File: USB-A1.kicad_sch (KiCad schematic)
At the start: 26 parts, among them J8 USB3_A, J9 USB3_A, U16 UCS2113-1-V/G4, U17 TPD4E02B04DQA, U18 TPD4E02B04DQA

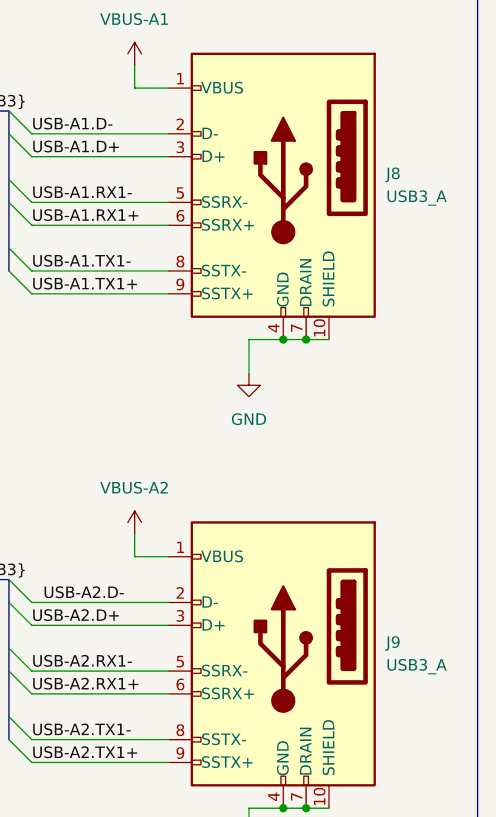
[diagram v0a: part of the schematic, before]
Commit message: TPS25762 EEPROM connector added
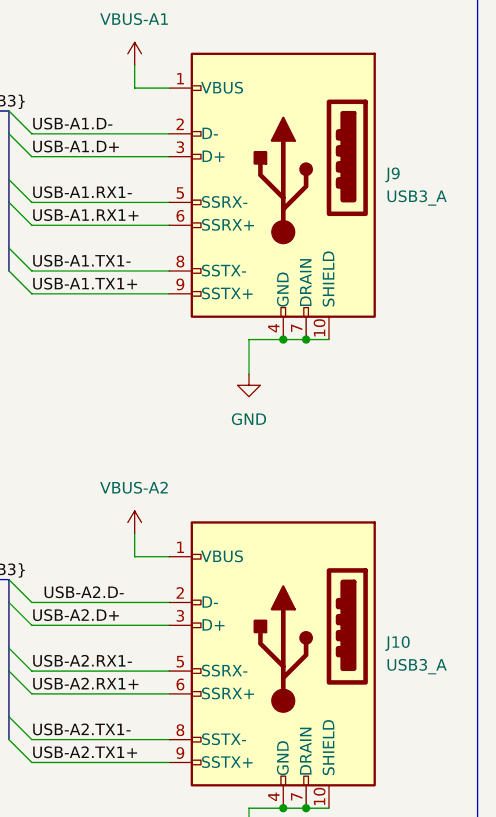
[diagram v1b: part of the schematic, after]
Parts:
- renumbered J9 to J10, J8 to J9
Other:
- title: (none) -> USB Hub
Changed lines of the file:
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@@
 	(generator_version "9.0")
 	(paper "A4")
+	(title_block
+		(title "USB Hub")
+	)
 	(rectangle
 		(start 15.24 71.12)
@@
 		(dnp no)
 		(fields_autoplaced yes)
-		(property "Reference" "J8"
+		(property "Reference" "J9"
 			(at 273.05 40.0049 0)
 			(effects
@@
 			(project ""
 				(path "/a2586c28-95f1-49e6-9254-37d7a8473e53/10c83c9e-05bd-4fa1-b7e1-a721413825c3"
-					(reference "J8")
+					(reference "J9")
 					(unit 1)
 				)
@@
 		(dnp no)
 		(fields_autoplaced yes)
-		(property "Reference" "J9"
+		(property "Reference" "J10"
 			(at 273.05 92.0749 0)
 			(effects
@@
 			(project "USB_hub"
 				(path "/a2586c28-95f1-49e6-9254-37d7a8473e53/10c83c9e-05bd-4fa1-b7e1-a721413825c3"
-					(reference "J9")
+					(reference "J10")
 					(unit 1)
 				)

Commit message: deleted duplicated capacitor
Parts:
- C77, C78, C79, C80: footprint (none) -> Capacitor_THT:C_Radial_D10.0mm_H16.0mm_P5.00mm
- C81: footprint (none) -> Capacitor_SMD:C_0402_1005Metric
- J10, J9: footprint (none) -> Connector_USB:USB3_A_Molex_48393-001
- JP2, JP3: footprint (none) -> Jumper:SolderJumper-2_P1.3mm_Open_Pad1.0x1.5mm
- JP4: footprint (none) -> Jumper:SolderJumper-3_P1.3mm_Open_RoundedPad1.0x1.5mm_NumberLabels
- R45, R46, R47, R48, R49, R50, R51: footprint (none) -> Resistor_SMD:R_0603_1608Metric
- TP5, TP6: footprint (none) -> TestPoint:TestPoint_THTPad_1.5x1.5mm_Drill0.7mm
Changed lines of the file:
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@@
 			)
 		)
-		(property "Footprint" ""
+		(property "Footprint" "Resistor_SMD:R_0603_1608Metric"
 			(at 54.61 92.202 90)
 			(effects
@@
 			)
 		)
-		(property "Footprint" ""
+		(property "Footprint" "Resistor_SMD:R_0603_1608Metric"
 			(at 29.972 35.56 90)
 			(effects
@@
 			)
 		)
-		(property "Footprint" ""
+		(property "Footprint" "Capacitor_THT:C_Radial_D10.0mm_H16.0mm_P5.00mm"
 			(at 108.9152 26.67 0)
 			(effects
@@
 			)
 		)
-		(property "Footprint" ""
+		(property "Footprint" "Connector_USB:USB3_A_Molex_48393-001"
 			(at 257.81 38.1 0)
 			(effects
@@
 			)
 		)
-		(property "Footprint" ""
+		(property "Footprint" "Capacitor_SMD:C_0402_1005Metric"
 			(at 124.1552 26.67 0)
 			(effects
@@
 			)
 		)
-		(property "Footprint" ""
+		(property "Footprint" "Resistor_SMD:R_0603_1608Metric"
 			(at 47.498 24.13 90)
 			(effects
@@
 			)
 		)
-		(property "Footprint" ""
+		(property "Footprint" "TestPoint:TestPoint_THTPad_1.5x1.5mm_Drill0.7mm"
 			(at 101.6 82.55 0)
 			(effects
@@
 			)
 		)
-		(property "Footprint" ""
+		(property "Footprint" "Capacitor_THT:C_Radial_D10.0mm_H16.0mm_P5.00mm"
 			(at 116.5352 26.67 0)
 			(effects
@@
 			)
 		)
-		(property "Footprint" ""
+		(property "Footprint" "Resistor_SMD:R_0603_1608Metric"
 			(at 100.33 46.482 90)
 			(effects
@@
 			)
 		)
-		(property "Footprint" ""
+		(property "Footprint" "TestPoint:TestPoint_THTPad_1.5x1.5mm_Drill0.7mm"
 			(at 80.01 82.55 0)
 			(effects
@@
 			)
 		)
-		(property "Footprint" ""
+		(property "Footprint" "Resistor_SMD:R_0603_1608Metric"
 			(at 88.9 47.498 90)
 			(effects
@@
 			)
 		)
-		(property "Footprint" ""
+		(property "Footprint" "Capacitor_THT:C_Radial_D10.0mm_H16.0mm_P5.00mm"
 			(at 93.6752 26.67 0)
 			(effects
@@
 			)
 		)
-		(property "Footprint" ""
+		(property "Footprint" "Capacitor_THT:C_Radial_D10.0mm_H16.0mm_P5.00mm"
 			(at 101.2952 26.67 0)
 			(effects
@@
 			)
 		)
-		(property "Footprint" ""
+		(property "Footprint" "Connector_USB:USB3_A_Molex_48393-001"
 			(at 257.81 90.17 0)
 			(effects
@@
 			)
 		)
-		(property "Footprint" ""
+		(property "Footprint" "Jumper:SolderJumper-2_P1.3mm_Open_Pad1.0x1.5mm"
 			(at 88.9 40.64 0)
 			(effects
@@
 			)
 		)
-		(property "Footprint" ""
+		(property "Footprint" "Resistor_SMD:R_0603_1608Metric"
 			(at 54.61 76.962 90)
 			(effects
@@
 			)
 		)
-		(property "Footprint" ""
+		(property "Footprint" "Jumper:SolderJumper-2_P1.3mm_Open_Pad1.0x1.5mm"
 			(at 88.9 43.18 0)
 			(effects
@@
 			)
 		)
-		(property "Footprint" ""
+		(property "Footprint" "Jumper:SolderJumper-3_P1.3mm_Open_RoundedPad1.0x1.5mm_NumberLabels"
 			(at 45.72 86.36 0)
 			(effects
@@
 			)
 		)
-		(property "Footprint" ""
+		(property "Footprint" "Resistor_SMD:R_0603_1608Metric"
 			(at 85.598 31.75 90)
 			(effects

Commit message: Minor fixes
Fixed unclear labelling of buses
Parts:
- R45, R46, R47, R48, R49, R50, R51: footprint Resistor_SMD:R_0603_1608Metric -> Resistor_SMD:R_0402_1005Metric
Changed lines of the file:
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@@
 			)
 		)
-		(property "Footprint" "Resistor_SMD:R_0603_1608Metric"
+		(property "Footprint" "Resistor_SMD:R_0402_1005Metric"
 			(at 54.61 92.202 90)
 			(effects
@@
 			)
 		)
-		(property "Footprint" "Resistor_SMD:R_0603_1608Metric"
+		(property "Footprint" "Resistor_SMD:R_0402_1005Metric"
 			(at 29.972 35.56 90)
 			(effects
@@
 			)
 		)
-		(property "Footprint" "Resistor_SMD:R_0603_1608Metric"
+		(property "Footprint" "Resistor_SMD:R_0402_1005Metric"
 			(at 47.498 24.13 90)
 			(effects
@@
 			)
 		)
-		(property "Footprint" "Resistor_SMD:R_0603_1608Metric"
+		(property "Footprint" "Resistor_SMD:R_0402_1005Metric"
 			(at 100.33 46.482 90)
 			(effects
@@
 			)
 		)
-		(property "Footprint" "Resistor_SMD:R_0603_1608Metric"
+		(property "Footprint" "Resistor_SMD:R_0402_1005Metric"
 			(at 88.9 47.498 90)
 			(effects
@@
 			)
 		)
-		(property "Footprint" "Resistor_SMD:R_0603_1608Metric"
+		(property "Footprint" "Resistor_SMD:R_0402_1005Metric"
 			(at 54.61 76.962 90)
 			(effects
@@
 			)
 		)
-		(property "Footprint" "Resistor_SMD:R_0603_1608Metric"
+		(property "Footprint" "Resistor_SMD:R_0402_1005Metric"
 			(at 85.598 31.75 90)
 			(effects

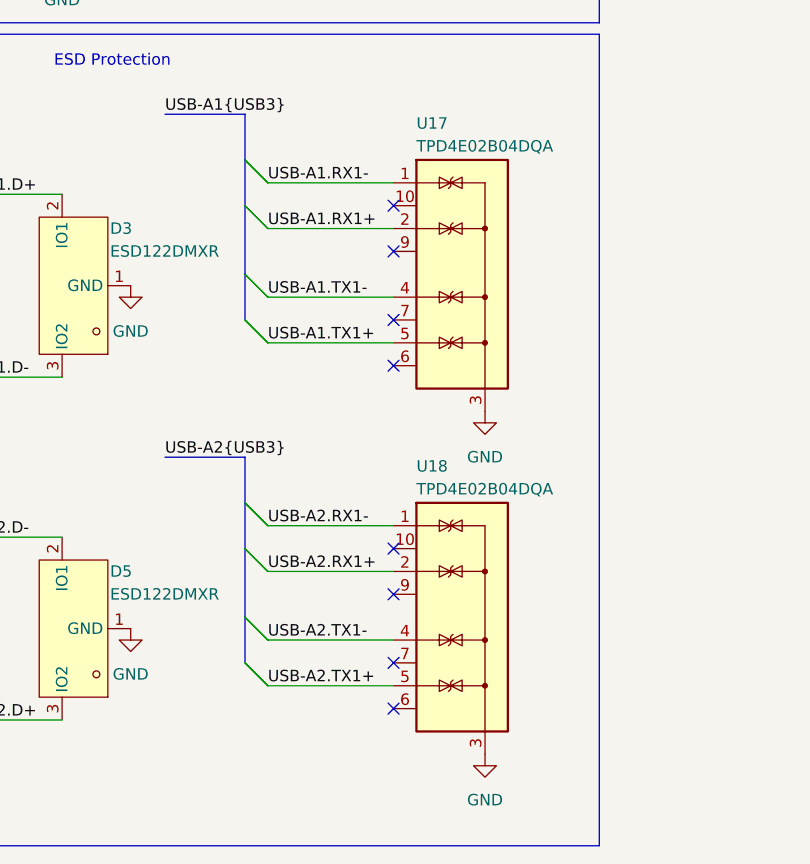
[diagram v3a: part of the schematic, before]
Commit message: Scheme fixes
Fixed wrong connection of SNS pin of U21
USB7206c symbol improved
R7's value fixed
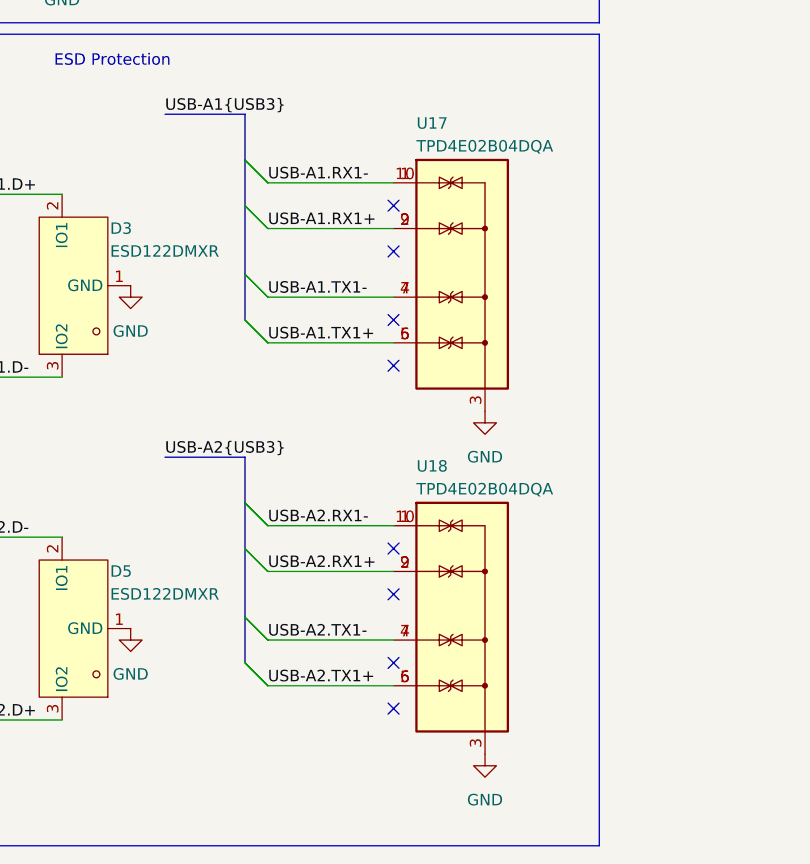
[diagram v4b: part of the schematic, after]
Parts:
- U17, U18: symbol Power_Protection:TPD4E02B04DQA -> Snapeda:TPD4E02B04DQA
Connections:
- net USB-A1.RX1+: now also U17.9 (NC)
- net USB-A1.RX1-: now also U17.10 (NC)
- net USB-A1.TX1+: now also U17.6 (NC)
- net USB-A1.TX1-: now also U17.7 (NC)
- net USB-A2.RX1+: now also U18.9 (NC)
- net USB-A2.RX1-: now also U18.10 (NC)
- net USB-A2.TX1+: now also U18.6 (NC)
- net USB-A2.TX1-: now also U18.7 (NC)
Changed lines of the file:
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@@
 	)
 	(symbol
-		(lib_id "Power_Protection:TPD4E02B04DQA")
+		(lib_id "Snapeda:TPD4E02B04DQA")
 		(at 106.68 170.18 0)
 		(unit 1)
@@
 	)
 	(symbol
-		(lib_id "Power_Protection:TPD4E02B04DQA")
+		(lib_id "Snapeda:TPD4E02B04DQA")
 		(at 106.68 132.08 0)
 		(unit 1)

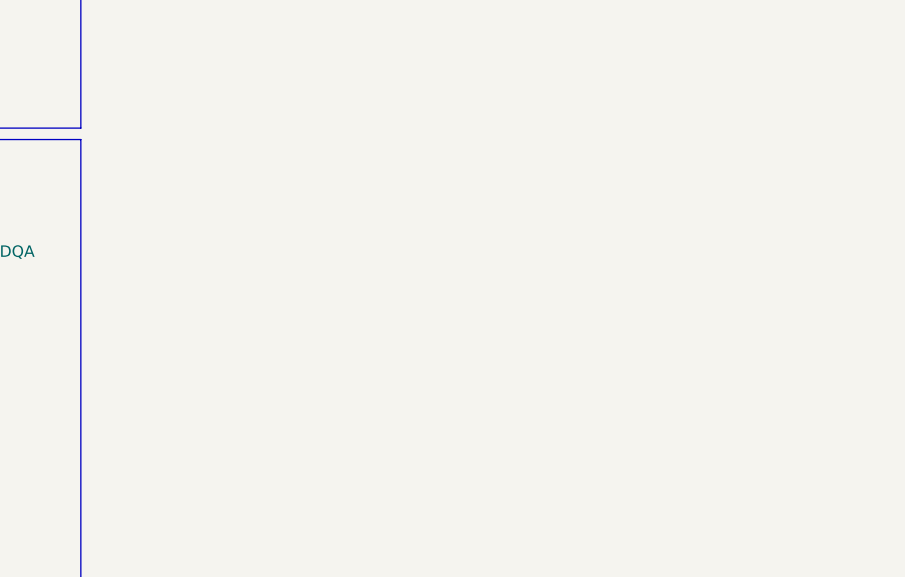
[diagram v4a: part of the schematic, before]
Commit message: MCP19035 changed to MP8795
TPS7A4701xRGW to AP7361C-33E
Led Indicator added
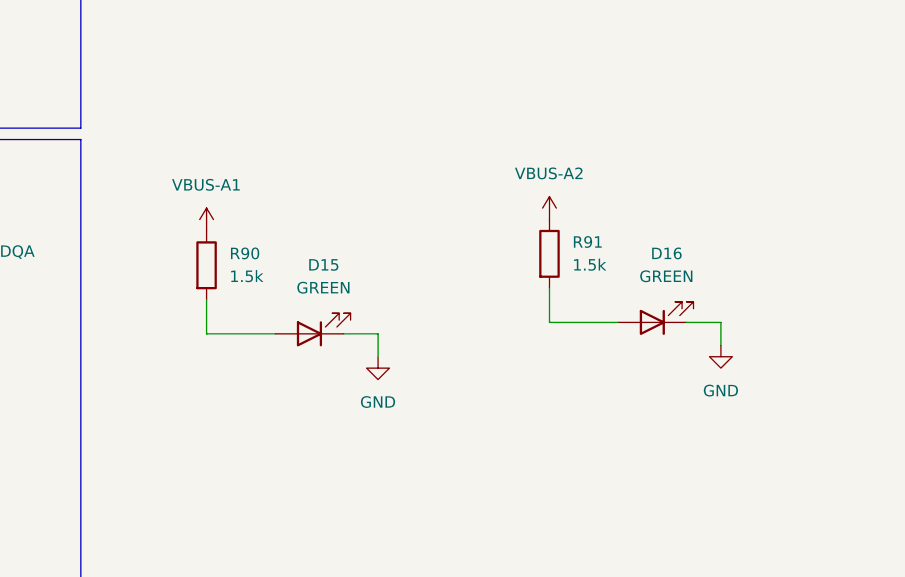
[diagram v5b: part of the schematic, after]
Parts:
- added D15, D16: GREEN, symbol Device:LED
- added R90, R91: 1.5k, symbol Device:R
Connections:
- net GND: now also D15.1 (K), D16.1 (K)
- net VBUS-A1: now also R90.1
- net VBUS-A2: now also R91.1
- new net: D16.2 (A), R91.2
- new net: D15.2 (A), R90.2

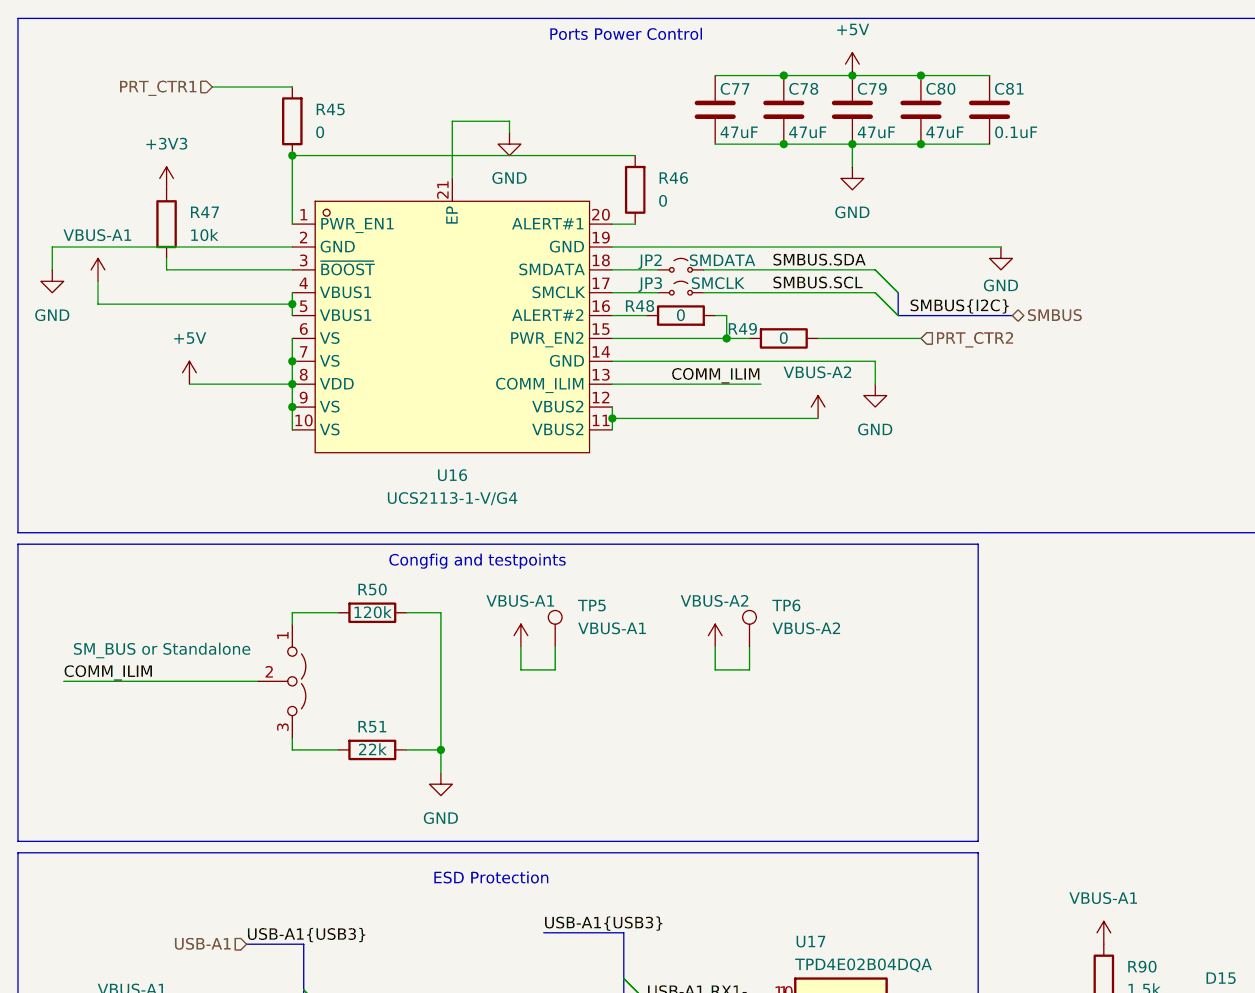
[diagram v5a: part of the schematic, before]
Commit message: I2C Addresses added to scheme
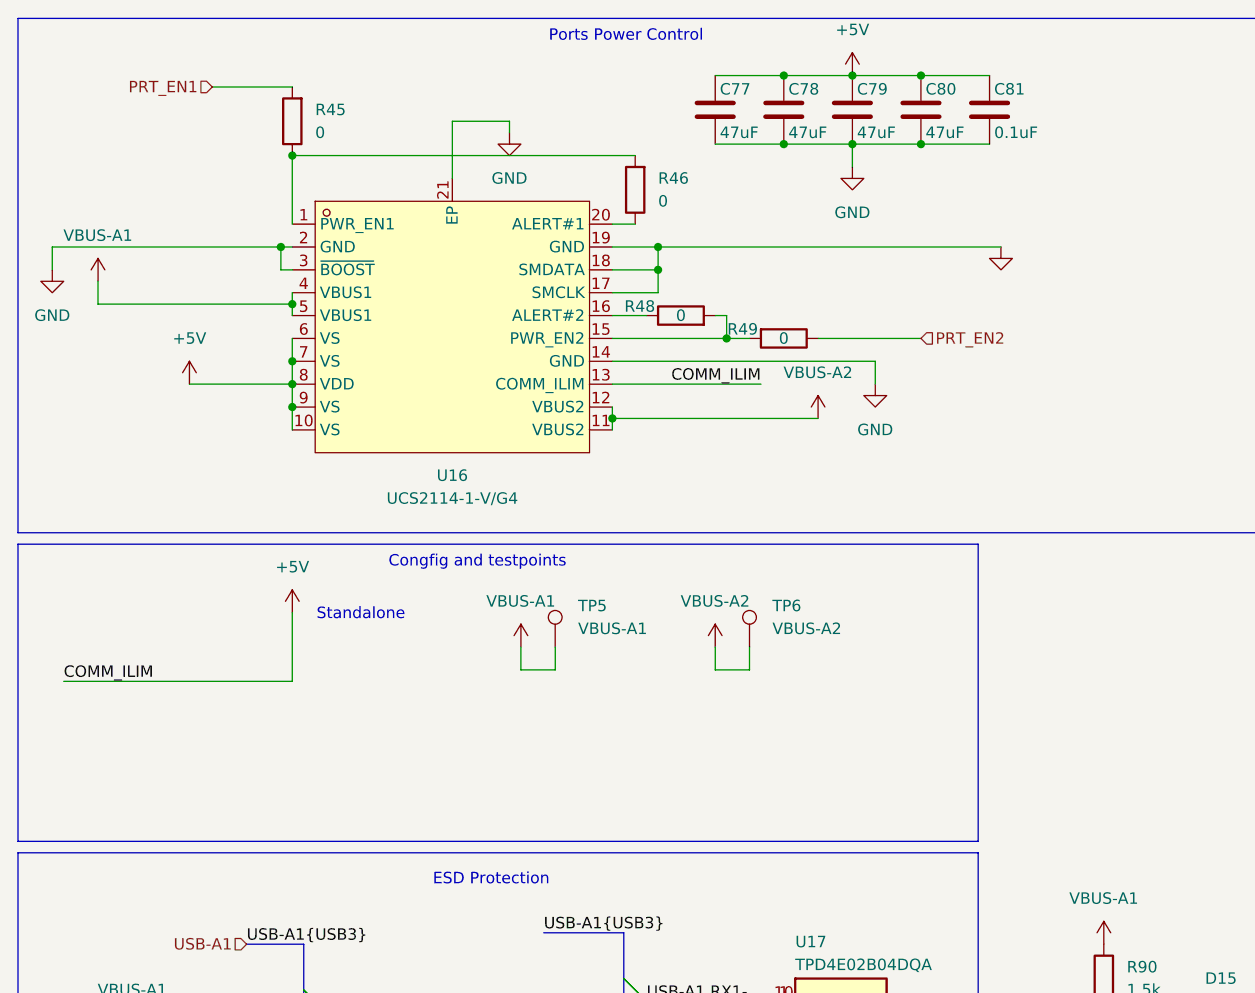
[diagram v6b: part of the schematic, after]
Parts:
- removed JP2: SMDATA, Jumper:SolderJumper-2_P1.3mm_Open_Pad1.0x1.5mm, symbol Jumper:Jumper_2_Small_Open
- removed JP3: SMCLK, Jumper:SolderJumper-2_P1.3mm_Open_Pad1.0x1.5mm, symbol Jumper:Jumper_2_Small_Open
- removed JP4: SM_BUS or Standalone, Jumper:SolderJumper-3_P1.3mm_Open_RoundedPad1.0x1.5mm_NumberLabels, symbol Jumper:Jumper_3_Open
- removed R47: 10k, Resistor_SMD:R_0402_1005Metric, symbol Device:R
- removed R50: 120k, Resistor_SMD:R_0402_1005Metric, symbol Device:R
- removed R51: 22k, Resistor_SMD:R_0402_1005Metric, symbol Device:R
- U16: value UCS2113-1-V/G4 -> UCS2114-1-V/G4
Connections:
- net COMM_ILIM is gone; now on net +5V: U16.13 (COMM_ILIM)
- net GND: now also U16.17 (SMCLK), U16.18 (SMDATA), U16.3 (~{BOOST})
- net PRT_CTR1 renamed PRT_EN1
- net PRT_CTR2 renamed PRT_EN2
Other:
- note added: "Standalone"
